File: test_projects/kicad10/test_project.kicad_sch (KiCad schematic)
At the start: 3 parts

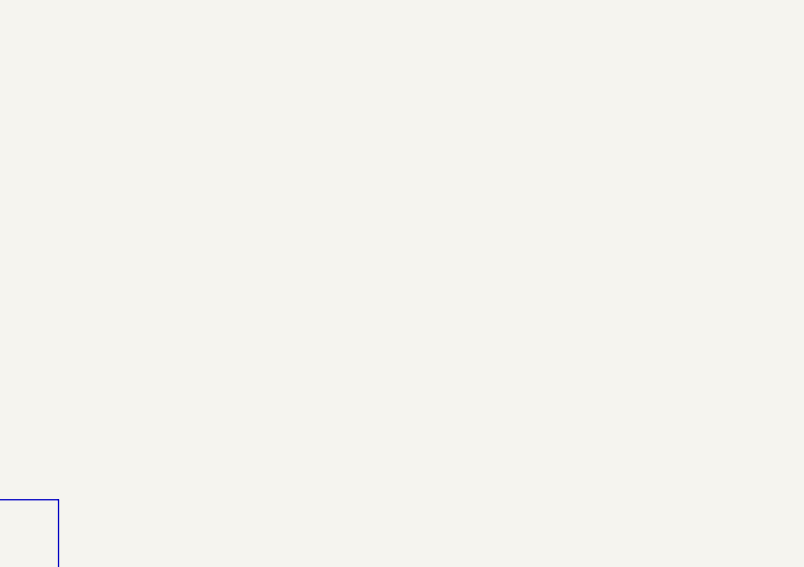
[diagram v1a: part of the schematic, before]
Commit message: [#89355] test_projects: K10: Add additional features
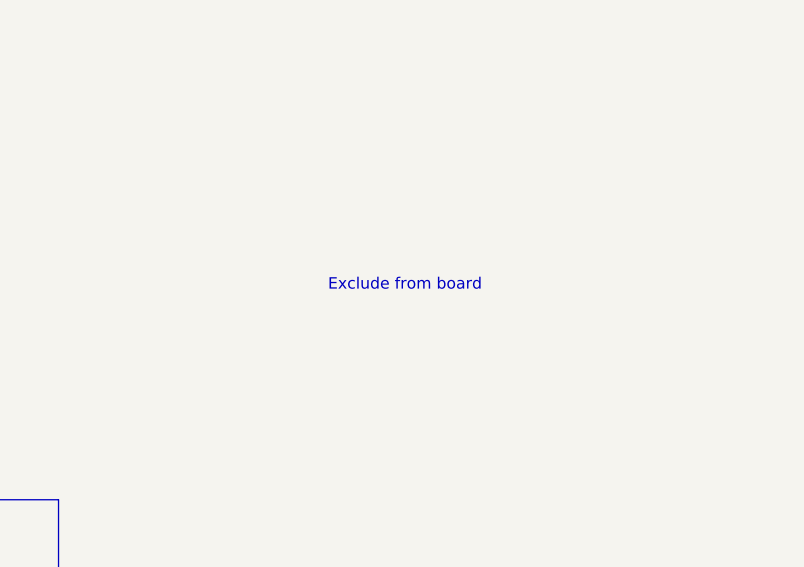
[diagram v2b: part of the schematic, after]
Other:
- note added: "Exclude from board"
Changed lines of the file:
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@@
 (kicad_sch
-	(version 20260101)
+	(version 20260306)
 	(generator "eeschema")
 	(generator_version "10.0")
@@
 		(exclude_from_sim no)
 		(at 243.078 105.41 0)
+		(effects
+			(font
+				(size 1.27 1.27)
+			)
+		)
+	)
+	(text "Exclude from board"
+		(exclude_from_sim no)
+		(at 350.52 94.234 0)
 		(effects
 			(font
@@
 		)
 	)
+	(rule_area
+		(exclude_from_sim no)
+		(in_bom yes)
+		(on_board no)
+		(dnp no)
+		(polyline
+			(pts
+				(xy 337.82 91.44) (xy 363.22 91.44) (xy 363.22 115.57) (xy 361.95 116.84) (xy 347.98 116.84) (xy 337.82 106.68)
+			)
+			(stroke
+				(width 0)
+				(type dash)
+			)
+			(fill
+				(type hatch)
+				(color 255 0 255 0.5019607843)
+			)
+		)
+	)
 	(netclass_flag ""
 		(length 2.54)
@@
 		)
 		(instances
-			(project ""
+			(project "test_project"
 				(path "/59f522e0-0cf7-48a6-bc09-47b340553d24"
 					(reference "H1")
@@
 		)
 		(instances
-			(project ""
+			(project "test_project"
 				(path "/59f522e0-0cf7-48a6-bc09-47b340553d24"
 					(reference "#SYM1")
@@
 		)
 		(instances
-			(project ""
+			(project "test_project"
 				(path "/59f522e0-0cf7-48a6-bc09-47b340553d24"
 					(reference "#PWR041")
